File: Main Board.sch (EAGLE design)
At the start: 19 parts, among them U1 TPS61030RSAR

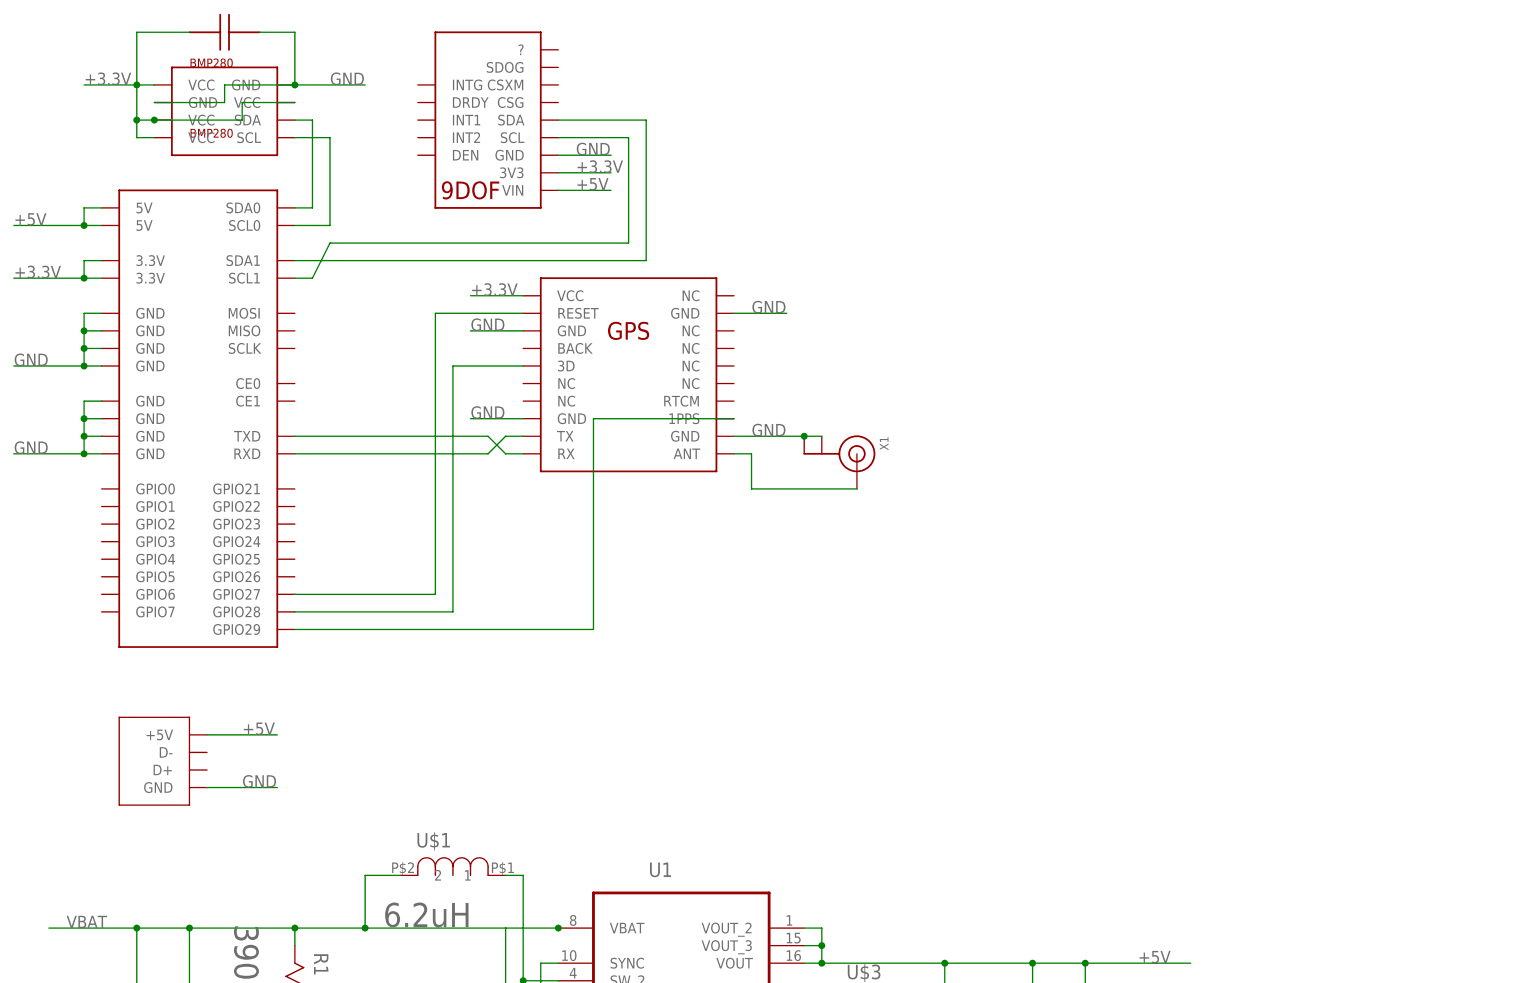
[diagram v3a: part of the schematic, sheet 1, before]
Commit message: Completed Motor Driver schematic
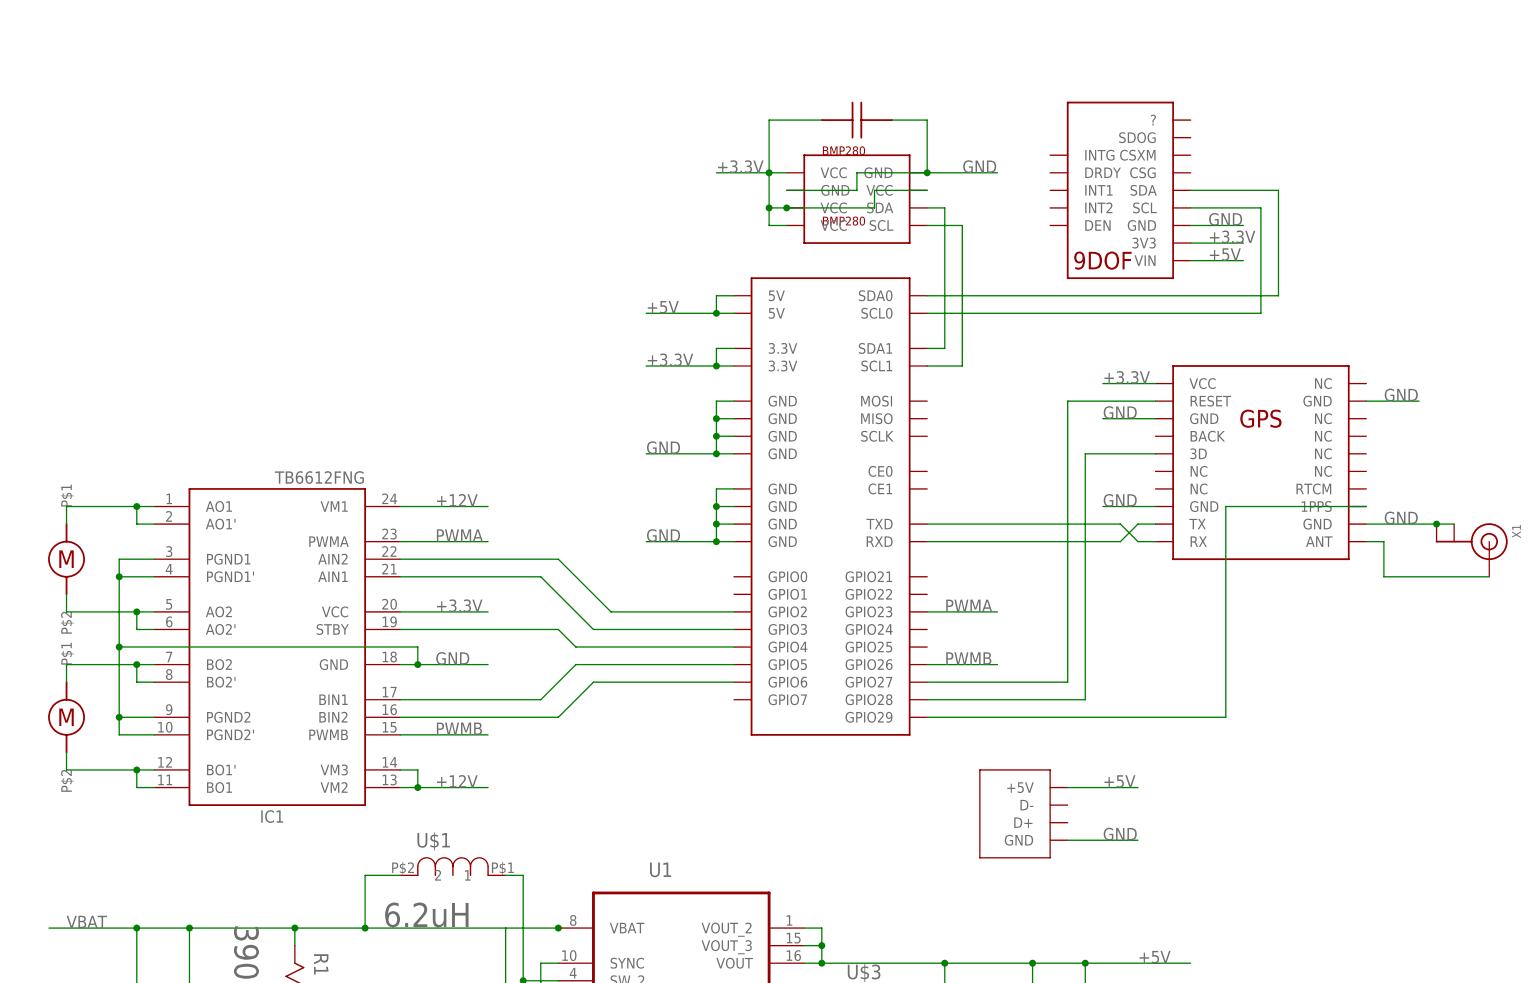
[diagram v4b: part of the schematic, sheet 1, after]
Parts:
- added IC1: TB6612FNG, Adafruit:TB6612FNG
- added U$15, U$16: MOTOR2, GoatFinder:MOTOR2
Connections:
- new net +12V: IC1.VM1, IC1.VM2, IC1.VM3
- new net N$15: IC1.AIN2, U$11.GPIO2
- new net N$16: IC1.AO1, IC1.AO1', U$15.P$1
- new net N$17: IC1.AO2, IC1.AO2', U$15.P$2
- new net N$18: IC1.BO2, IC1.BO2', U$16.P$1
- new net N$19: IC1.BO1, IC1.BO1', U$16.P$2
- new net N$20: IC1.AIN1, U$11.GPIO3
- new net N$21: IC1.STBY, U$11.GPIO4
- new net N$22: IC1.BIN1, U$11.GPIO5
- new net N$23: IC1.BIN2, U$11.GPIO6
- new net PWMA: IC1.PWMA, U$11.GPIO23
- new net PWMB: IC1.PWMB, U$11.GPIO26
- net +3.3V: now also IC1.VCC
- net GND: now also IC1.GND, IC1.PGND1, IC1.PGND1', IC1.PGND2, IC1.PGND2'
- net N$10: now also U$11.SCL1; no longer U$11.SCL0
- net N$12: now also U$11.SDA1; no longer U$11.SDA0
- net N$13: now also U$11.SDA0; no longer U$11.SDA1
- net N$14: now also U$11.SCL0; no longer U$11.SCL1
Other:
- moved on the sheet: X1

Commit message: Modified part placment
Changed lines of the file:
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@@
 <junction x="76.2" y="-22.86"/>
 <wire x1="60.96" y1="-22.86" x2="53.34" y2="-22.86" width="0.1524" layer="91"/>
-<wire x1="53.34" y1="-22.86" x2="40.64" y2="-22.86" width="0.1524" layer="91"/>
+<wire x1="53.34" y1="-22.86" x2="33.02" y2="-22.86" width="0.1524" layer="91"/>
 <wire x1="111.76" y1="-22.86" x2="170.18" y2="-22.86" width="0.1524" layer="91"/>
 <label x="43.18" y="-22.86" size="1.778" layer="95"/>
@@
 <wire x1="170.18" y1="-22.86" x2="182.88" y2="-22.86" width="0.1524" layer="91"/>
 <wire x1="182.88" y1="-22.86" x2="190.5" y2="-22.86" width="0.1524" layer="91"/>
-<wire x1="190.5" y1="-22.86" x2="205.74" y2="-22.86" width="0.1524" layer="91"/>
 <wire x1="60.96" y1="-5.08" x2="60.96" y2="-22.86" width="0.1524" layer="91"/>
 <junction x="60.96" y="-22.86"/>
@@
 <pinref part="U$12" gate="G$1" pin="P$2"/>
 <wire x1="190.5" y1="-10.16" x2="190.5" y2="-22.86" width="0.1524" layer="91"/>
-<junction x="190.5" y="-22.86"/>
 <pinref part="R2" gate="A" pin="1"/>
 <wire x1="167.64" y1="-15.24" x2="170.18" y2="-15.24" width="0.1524" layer="91"/>
@@
 <pinref part="U$7" gate="G$1" pin="P$1"/>
 <wire x1="60.96" y1="15.24" x2="53.34" y2="15.24" width="0.1524" layer="91"/>
-<wire x1="53.34" y1="15.24" x2="40.64" y2="15.24" width="0.1524" layer="91"/>
+<wire x1="53.34" y1="15.24" x2="33.02" y2="15.24" width="0.1524" layer="91"/>
 <wire x1="60.96" y1="15.24" x2="60.96" y2="5.08" width="0.1524" layer="91"/>
 <junction x="60.96" y="15.24"/>

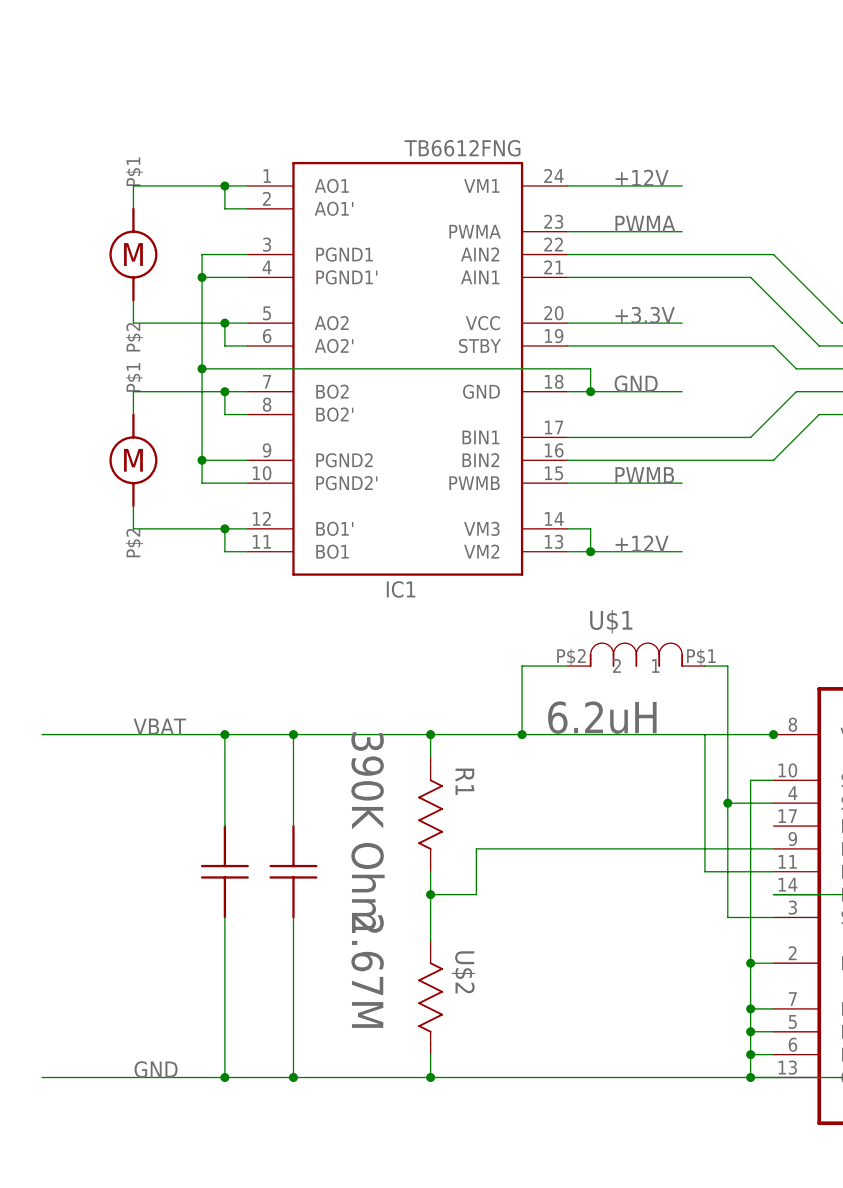
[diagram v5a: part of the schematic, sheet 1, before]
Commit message: Reduced Board Size and added Ground Planes
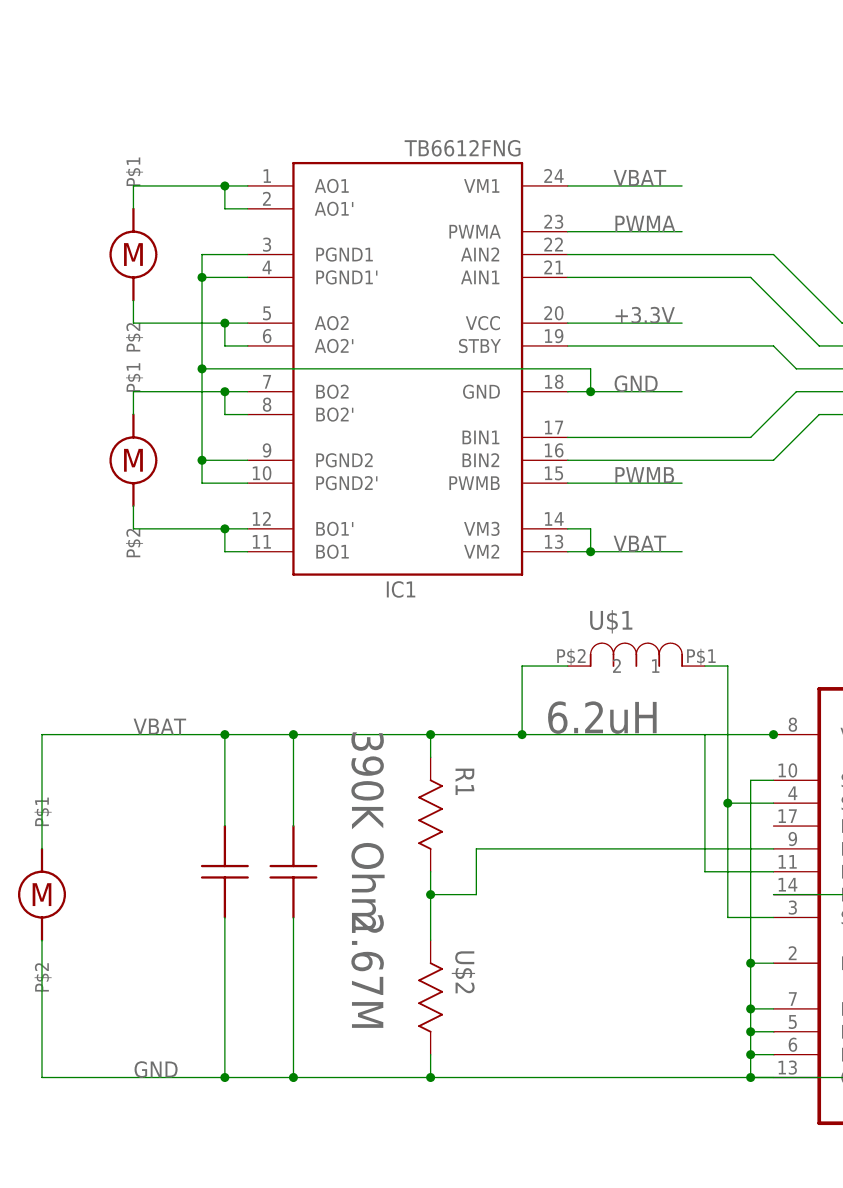
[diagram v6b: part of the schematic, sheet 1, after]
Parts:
- added U$17: MOTOR2, GoatFinder:MOTOR2
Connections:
- removed net +12V: IC1.VM1, IC1.VM2, IC1.VM3
- net GND: now also U$17.P$2
- net VBAT: now also IC1.VM1, IC1.VM2, IC1.VM3, U$17.P$1
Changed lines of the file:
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@@
 <part name="U$15" library="GoatFinder" deviceset="MOTOR2" device=""/>
 <part name="U$16" library="GoatFinder" deviceset="MOTOR2" device=""/>
+<part name="U$17" library="GoatFinder" deviceset="MOTOR2" device=""/>
 </parts>
 <sheets>
@@
 <instance part="U$15" gate="G$1" x="43.18" y="68.58"/>
 <instance part="U$16" gate="G$1" x="43.18" y="45.72"/>
+<instance part="U$17" gate="G$1" x="33.02" y="-2.54"/>
 </instances>
 <busses>
@@
 <wire x1="170.18" y1="-15.24" x2="170.18" y2="-22.86" width="0.1524" layer="91"/>
 <junction x="170.18" y="-22.86"/>
+<pinref part="U$17" gate="G$1" pin="P$2"/>
+<wire x1="33.02" y1="-7.62" x2="33.02" y2="-22.86" width="0.1524" layer="91"/>
 </segment>
 <segment>
@@
 <wire x1="86.36" y1="22.86" x2="86.36" y2="15.24" width="0.1524" layer="91"/>
 <junction x="86.36" y="15.24"/>
+<pinref part="U$17" gate="G$1" pin="P$1"/>
+<wire x1="33.02" y1="15.24" x2="33.02" y2="2.54" width="0.1524" layer="91"/>
+</segment>
+<segment>
+<pinref part="IC1" gate="G$1" pin="VM3"/>
+<wire x1="91.44" y1="38.1" x2="93.98" y2="38.1" width="0.1524" layer="91"/>
+<wire x1="93.98" y1="38.1" x2="93.98" y2="35.56" width="0.1524" layer="91"/>
+<pinref part="IC1" gate="G$1" pin="VM2"/>
+<wire x1="93.98" y1="35.56" x2="91.44" y2="35.56" width="0.1524" layer="91"/>
+<wire x1="93.98" y1="35.56" x2="104.14" y2="35.56" width="0.1524" layer="91"/>
+<junction x="93.98" y="35.56"/>
+<label x="96.52" y="35.56" size="1.778" layer="95"/>
+</segment>
+<segment>
+<pinref part="IC1" gate="G$1" pin="VM1"/>
+<wire x1="91.44" y1="76.2" x2="104.14" y2="76.2" width="0.1524" layer="91"/>
+<label x="96.52" y="76.2" size="1.778" layer="95"/>
 </segment>
 </net>
@@
 </segment>
 </net>
-<net name="+12V" class="0">
-<segment>
-<pinref part="IC1" gate="G$1" pin="VM1"/>
-<wire x1="91.44" y1="76.2" x2="104.14" y2="76.2" width="0.1524" layer="91"/>
-<label x="96.52" y="76.2" size="1.778" layer="95"/>
-</segment>
-<segment>
-<pinref part="IC1" gate="G$1" pin="VM3"/>
-<wire x1="91.44" y1="38.1" x2="93.98" y2="38.1" width="0.1524" layer="91"/>
-<wire x1="93.98" y1="38.1" x2="93.98" y2="35.56" width="0.1524" layer="91"/>
-<pinref part="IC1" gate="G$1" pin="VM2"/>
-<wire x1="93.98" y1="35.56" x2="91.44" y2="35.56" width="0.1524" layer="91"/>
-<wire x1="93.98" y1="35.56" x2="104.14" y2="35.56" width="0.1524" layer="91"/>
-<junction x="93.98" y="35.56"/>
-<label x="96.52" y="35.56" size="1.778" layer="95"/>
-</segment>
-</net>

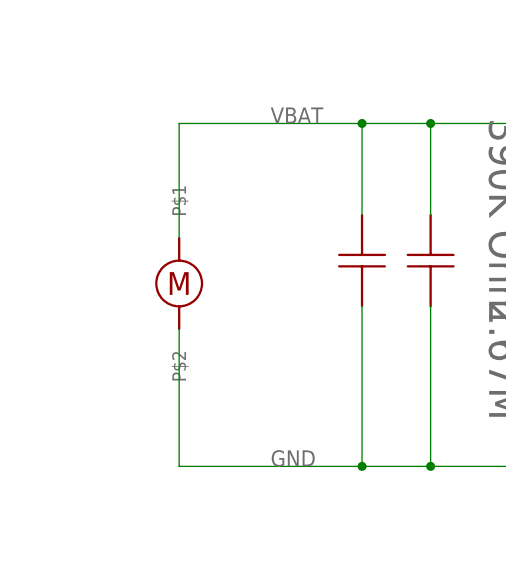
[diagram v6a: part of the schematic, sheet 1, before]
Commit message: Components in place, beginning traces.
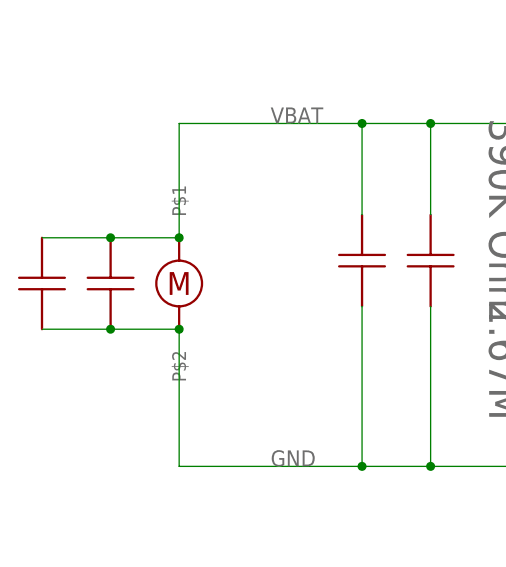
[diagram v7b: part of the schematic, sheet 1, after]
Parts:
- added U$18, U$19: 220, GoatFinder:220
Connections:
- net GND: now also U$18.P$2, U$19.P$2
- net VBAT: now also U$18.P$1, U$19.P$1
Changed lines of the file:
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@@
 <part name="U$16" library="GoatFinder" deviceset="MOTOR2" device=""/>
 <part name="U$17" library="GoatFinder" deviceset="MOTOR2" device=""/>
+<part name="U$18" library="GoatFinder" deviceset="220" device=""/>
+<part name="U$19" library="GoatFinder" deviceset="220" device=""/>
 </parts>
 <sheets>
@@
 <instance part="U$16" gate="G$1" x="43.18" y="45.72"/>
 <instance part="U$17" gate="G$1" x="33.02" y="-2.54"/>
+<instance part="U$18" gate="G$1" x="25.4" y="-2.54"/>
+<instance part="U$19" gate="G$1" x="17.78" y="-2.54"/>
 </instances>
 <busses>
@@
 <pinref part="U$17" gate="G$1" pin="P$2"/>
 <wire x1="33.02" y1="-7.62" x2="33.02" y2="-22.86" width="0.1524" layer="91"/>
+<pinref part="U$19" gate="G$1" pin="P$2"/>
+<pinref part="U$18" gate="G$1" pin="P$2"/>
+<wire x1="17.78" y1="-7.62" x2="25.4" y2="-7.62" width="0.1524" layer="91"/>
+<wire x1="25.4" y1="-7.62" x2="33.02" y2="-7.62" width="0.1524" layer="91"/>
+<junction x="25.4" y="-7.62"/>
+<junction x="33.02" y="-7.62"/>
 </segment>
 <segment>
@@
 <pinref part="U$17" gate="G$1" pin="P$1"/>
 <wire x1="33.02" y1="15.24" x2="33.02" y2="2.54" width="0.1524" layer="91"/>
-</segment>
-<segment>
+<pinref part="U$19" gate="G$1" pin="P$1"/>
+<pinref part="U$18" gate="G$1" pin="P$1"/>
+<wire x1="17.78" y1="2.54" x2="25.4" y2="2.54" width="0.1524" layer="91"/>
+<wire x1="25.4" y1="2.54" x2="33.02" y2="2.54" width="0.1524" layer="91"/>
+<junction x="25.4" y="2.54"/>
+<junction x="33.02" y="2.54"/>
+</segment>
+<segment>
